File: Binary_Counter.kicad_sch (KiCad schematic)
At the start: 37 parts, among them J2 Conn_01x03_Pin, SW2 SW_MEC_5E, U1 CH32V003FxUx

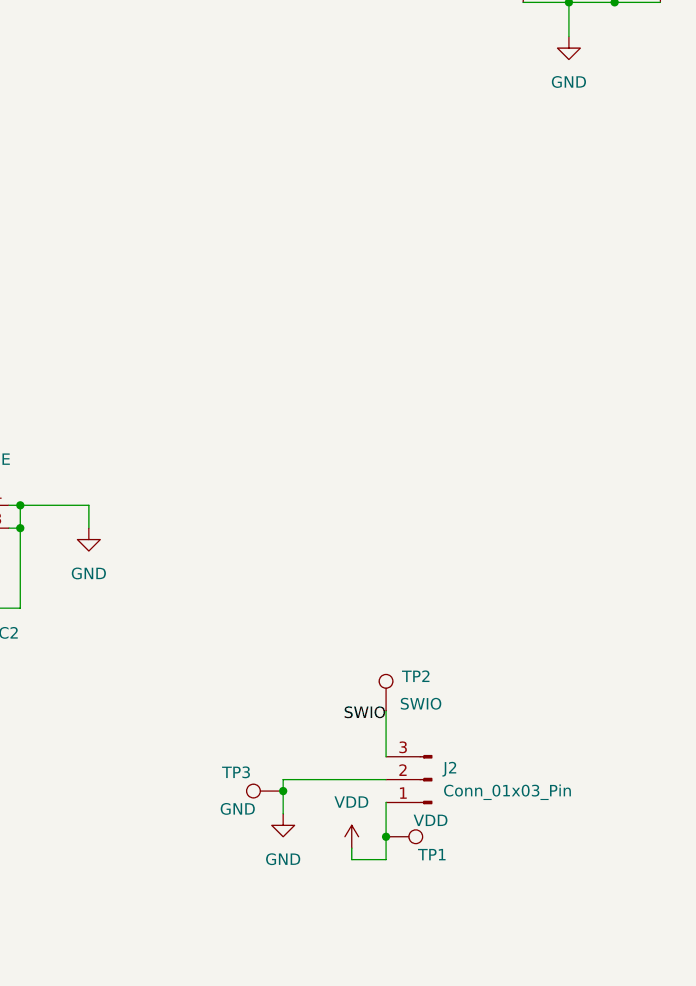
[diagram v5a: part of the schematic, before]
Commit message: add 3V3 LDO
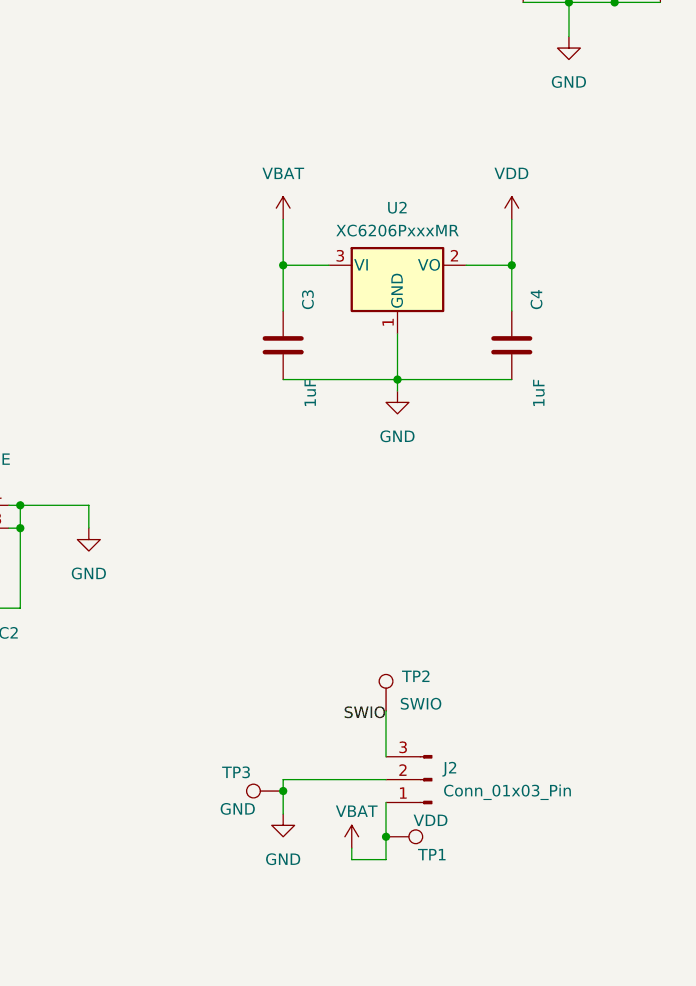
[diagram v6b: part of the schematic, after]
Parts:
- added C3, C4: 1uF, Capacitor_SMD:C_0805_2012Metric_Pad1.18x1.45mm_HandSolder, symbol Device:C
- added U2: XC6206PxxxMR, Package_TO_SOT_SMD:SOT-23-3, symbol Regulator_Linear:XC6206PxxxMR
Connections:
- net GND: now also C3.1, C4.1, U2.1 (GND)
- net VDD: now also C4.2, U2.2 (VO); no longer J2.1 (Pin_1), TP1.1
- new net VBAT: C3.2, J2.1 (Pin_1), TP1.1, U2.3 (VI)

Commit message: place and route LDO
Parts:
- H1, H2, H3, H4: footprint MountingHole:MountingHole_4mm_Pad -> MountingHole:MountingHole_2.2mm_M2
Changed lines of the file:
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@@
 			)
 		)
-		(property "Footprint" "MountingHole:MountingHole_4mm_Pad"
+		(property "Footprint" "MountingHole:MountingHole_2.2mm_M2"
 			(at 231.14 26.67 0)
 			(effects
@@
 			)
 		)
-		(property "Footprint" "MountingHole:MountingHole_4mm_Pad"
+		(property "Footprint" "MountingHole:MountingHole_2.2mm_M2"
 			(at 241.3 26.67 0)
 			(effects
@@
 			)
 		)
-		(property "Footprint" "MountingHole:MountingHole_4mm_Pad"
+		(property "Footprint" "MountingHole:MountingHole_2.2mm_M2"
 			(at 226.06 26.67 0)
 			(effects
@@
 			)
 		)
-		(property "Footprint" "MountingHole:MountingHole_4mm_Pad"
+		(property "Footprint" "MountingHole:MountingHole_2.2mm_M2"
 			(at 236.22 26.67 0)
 			(effects
